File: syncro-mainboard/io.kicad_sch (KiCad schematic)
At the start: 14 parts, among them J4 Micro_SD_Card_Det1, SW3 SW_USER, U7 EMIF06-MSD02N16

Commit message: Correct SMD5050 LED rotation
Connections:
- net +3.3V: now also D12.4 (GA), D12.5 (RA), D12.6 (BA); no longer D12.1 (GA), D12.2 (RA), D12.3 (BA)
- net LED_B_X: now also D12.1 (BK); no longer D12.4 (BK)
- net LED_G_X: now also D12.3 (GK); no longer D12.6 (GK)
- net LED_R_X: now also D12.2 (RK); no longer D12.5 (RK)

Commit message: Syncro mainboard rev 2
* Migrate I2C to I2C5 on SOM pins 132/133
* Use correctly reversed LED footprint
* Use updated rear graphics
* Set SOM to be assembled at JLC
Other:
- title: System IO -> Syncro FFB Interceptor
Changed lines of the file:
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@@
 	(paper "USLetter")
 	(title_block
-		(title "System IO")
-		(date "2026-08-25")
-		(rev "1")
+		(title "Syncro FFB Interceptor")
+		(date "2026-10-23")
+		(rev "2")
 		(company "Deadband Inc.")
 	)

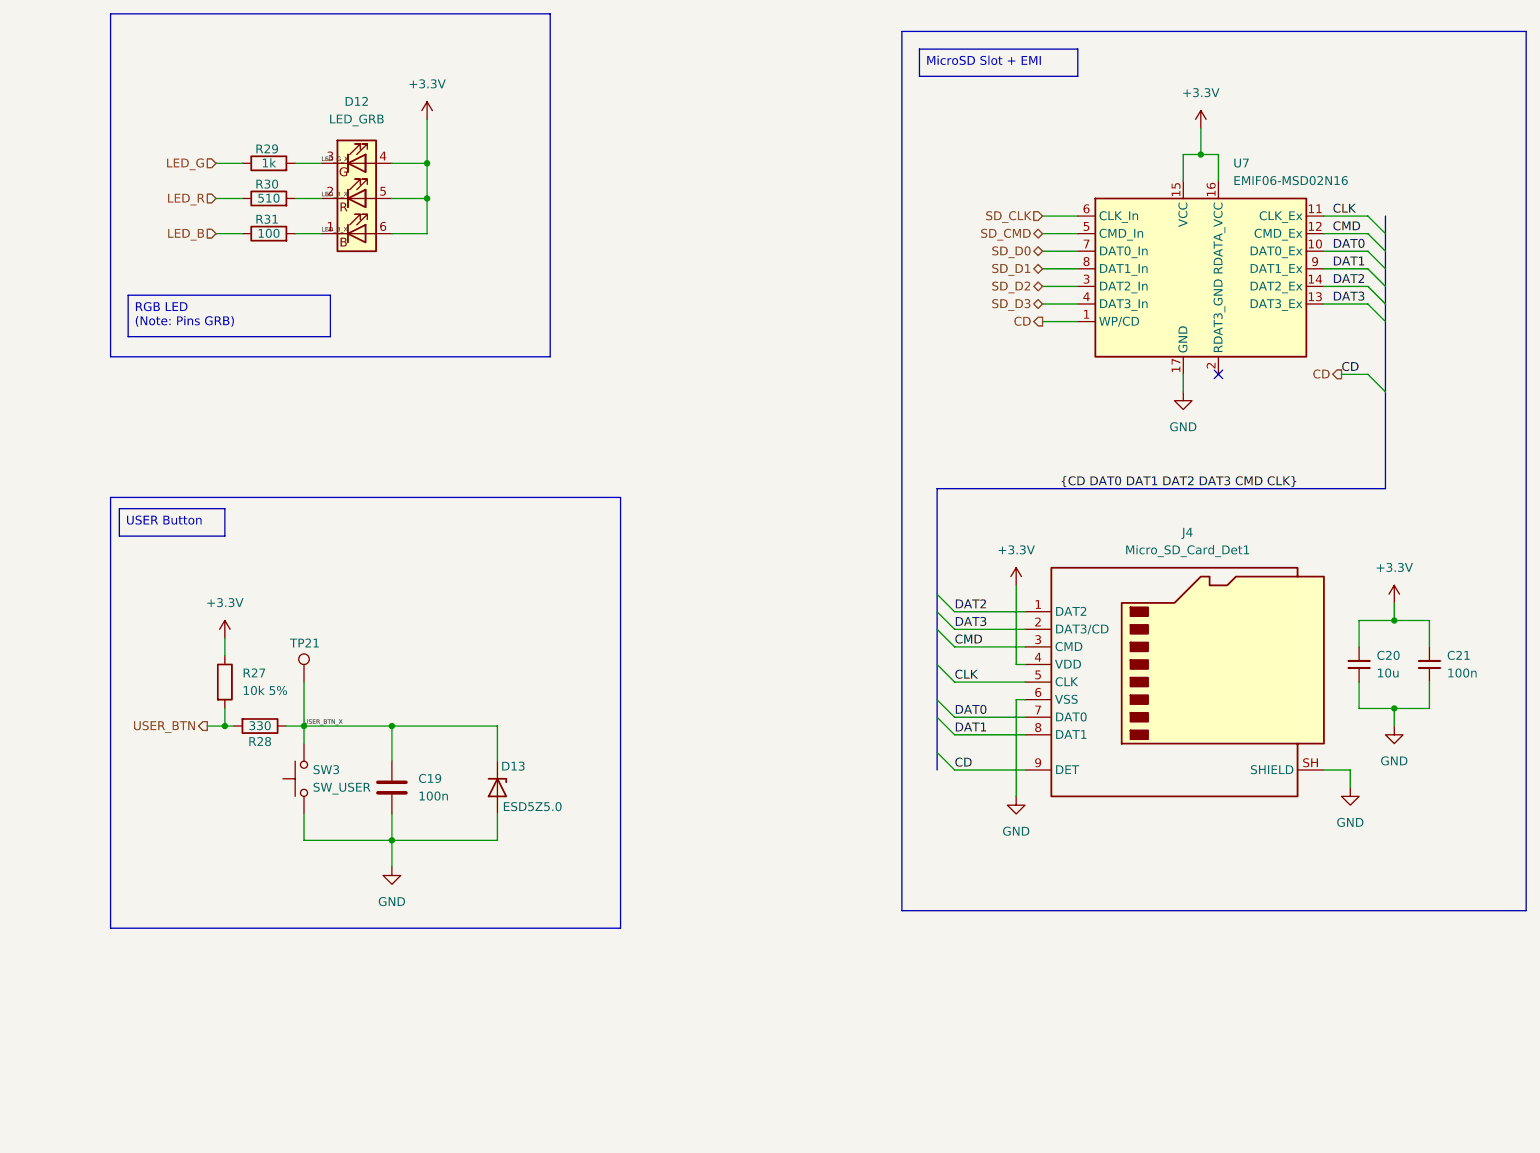
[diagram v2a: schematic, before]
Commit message: Syncro mainboard rev 3
* Add XL-1615 accent RGB LEDs D16-D18 on TIM8
* Add R48-R56 next to the LEDs and rework their shared +3.3V feed
* Add In2 GND return plane under the USB-C connector for TP5/TP6
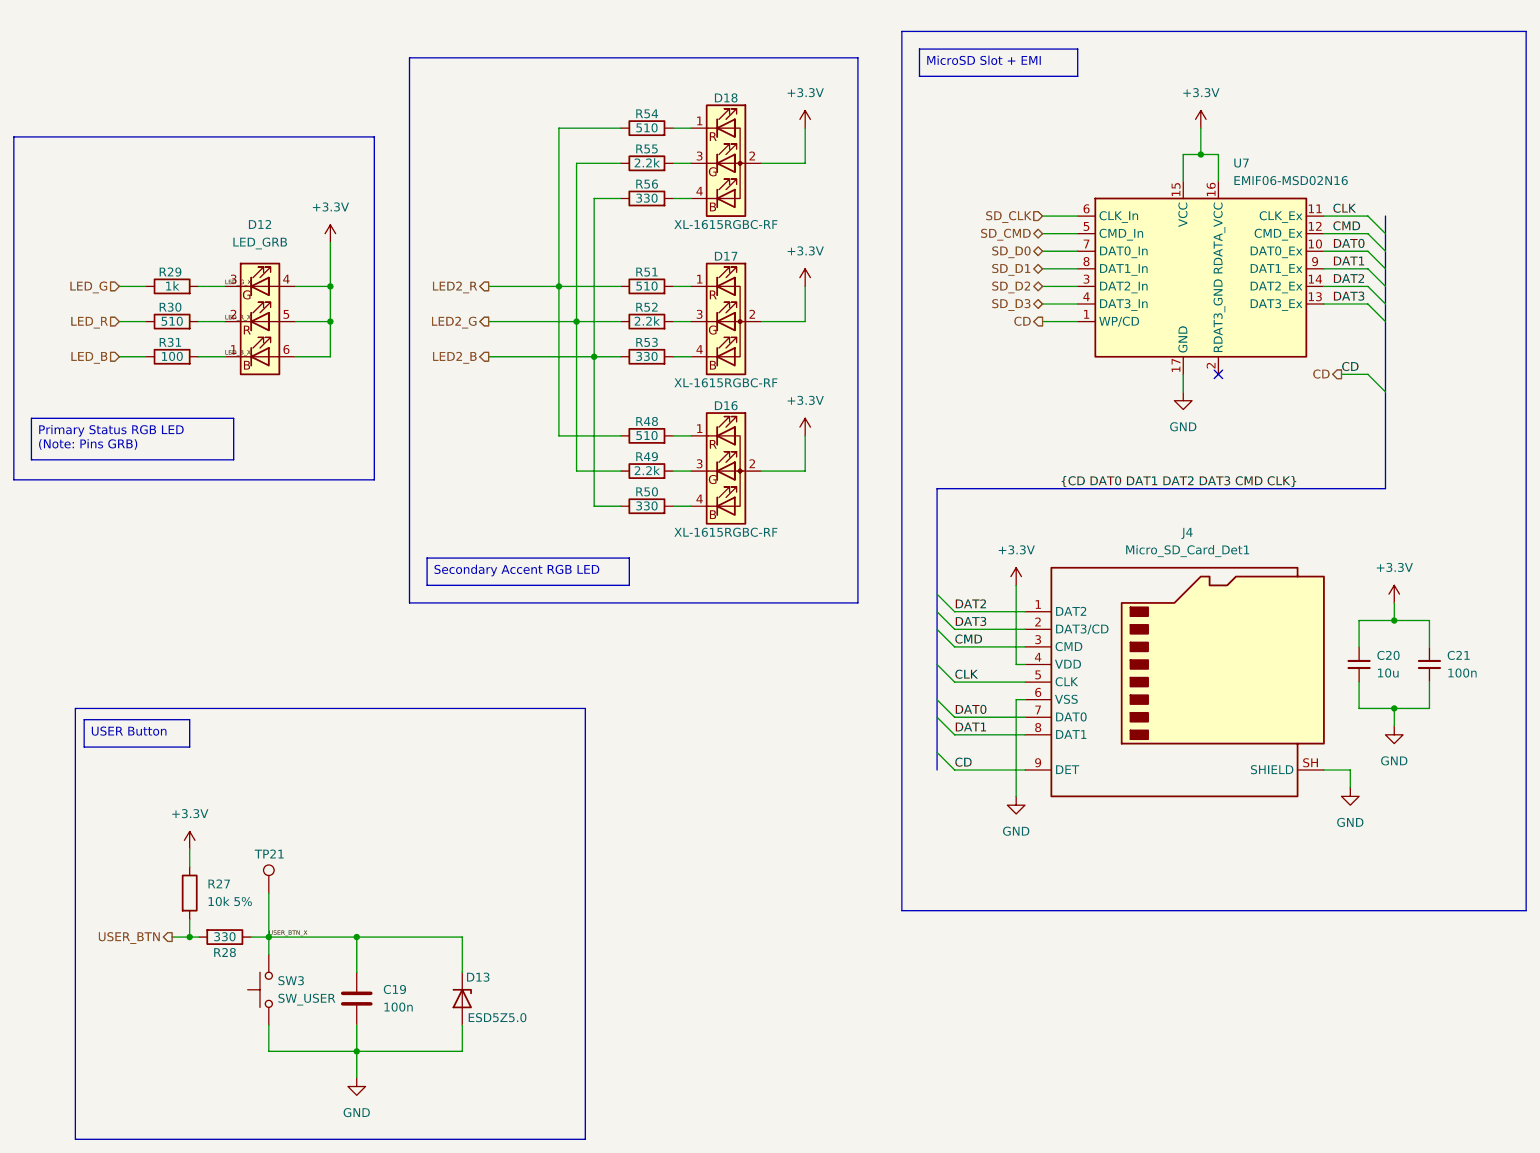
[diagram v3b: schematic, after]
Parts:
- added D16, D17, D18: XL-1615RGBC-RF, dbl-ic:LED_RGB_XINGLIGHT_XL-1615RGBC, symbol Device:LED_RAGB
- added R48, R51, R54: 510, Resistor_SMD:R_0402_1005Metric, symbol Device:R
- added R49, R52, R55: 2.2k, Resistor_SMD:R_0402_1005Metric, symbol Device:R
- added R50, R53, R56: 330, Resistor_SMD:R_0402_1005Metric, symbol Device:R
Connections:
- net +3.3V: now also D16.2 (A), D17.2 (A), D18.2 (A)
- new net: D18.3 (GK), R55.2
- new net: D17.4 (BK), R53.2
- new net: D18.1 (RK), R54.2
- new net: D18.4 (BK), R56.2
- new net: D17.3 (GK), R52.2
- new net: D17.1 (RK), R51.2
- new net: D16.3 (GK), R49.2
- new net: D16.4 (BK), R50.2
- new net: D16.1 (RK), R48.2
- new net LED2_B: R50.1, R53.1, R56.1
- new net LED2_G: R49.1, R52.1, R55.1
- new net LED2_R: R48.1, R51.1, R54.1
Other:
- moved on the sheet: C19, D12, D13, R27, R28, R29, R30, R31, SW3, TP21
